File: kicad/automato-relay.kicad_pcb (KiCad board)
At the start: 2 copper layers, 308 x 75 mm, 51 parts, among them J1 TE-3-213598-4, J2 Screw_Terminal_01x03, J3 TE-3-213598-4, J4 Screw_Terminal_01x05, J5 TE-3-213598-4, J6 TE-3-213598-4, J7 Screw_Terminal_01x05, J8 TE-3-213598-4, K1 G5LE-14, K2 G5LE-14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

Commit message: layout: minor changes to appease DRC
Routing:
- net ACE: track 445.5 -> 448.6 mm
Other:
- net class EARTH: trace_width 0.25 -> 5; via_dia 0.8 -> 2; via_drill 0.4 -> 1
- net class HV: clearance 1.75 -> 1; trace_width 8 -> 5
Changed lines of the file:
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@@
     (thickness 1.6)
     (drawings 20)
-    (tracks 259)
+    (tracks 263)
     (zones 0)
     (modules 51)
@@
   (net_class EARTH ""
     (clearance 1)
-    (trace_width 0.25)
-    (via_dia 0.8)
-    (via_drill 0.4)
+    (trace_width 5)
+    (via_dia 2)
+    (via_drill 1)
     (uvia_dia 0.3)
     (uvia_drill 0.1)
@@
   )
   (net_class HV ""
-    (clearance 1.75)
-    (trace_width 8)
+    (clearance 1)
+    (trace_width 5)
     (via_dia 2)
     (via_drill 1)
@@
   (segment (start 34.08 152.92) (end 31.5 155.5) (width 2) (layer F.Cu) (net 9))
   (segment (start 44 152.92) (end 34.08 152.92) (width 2) (layer F.Cu) (net 9))
-  (segment (start 21.800001 163.800001) (end 25 167) (width 3) (layer F.Cu) (net 10))
-  (segment (start 25 102) (end 21.800001 105.199999) (width 3) (layer F.Cu) (net 10))
-  (segment (start 21.800001 105.199999) (end 21.800001 163.800001) (width 3) (layer F.Cu) (net 10))
   (segment (start 75 161) (end 75 153.38) (width 5) (layer F.Cu) (net 10))
   (segment (start 135 161) (end 135 153.38) (width 5) (layer F.Cu) (net 10))
@@
   (segment (start 44 158) (end 44 160) (width 3) (layer F.Cu) (net 10))
   (segment (start 325.47499 164.52501) (end 323 167) (width 3) (layer F.Cu) (net 10))
-  (segment (start 325.47499 104.47499) (end 325.47499 164.52501) (width 3) (layer F.Cu) (net 10))
-  (segment (start 323 102) (end 325.47499 104.47499) (width 3) (layer F.Cu) (net 10))
+  (segment (start 325.47499 104.47499) (end 325.47499 164.52501) (width 2) (layer F.Cu) (net 10))
+  (segment (start 25 102) (end 22.75 102) (width 2) (layer F.Cu) (net 10))
+  (segment (start 324.828432 102.99999) (end 325.97499 104.146548) (width 2) (layer F.Cu) (net 10))
+  (segment (start 323.99999 102.99999) (end 324.828432 102.99999) (width 2) (layer F.Cu) (net 10))
+  (segment (start 323 102) (end 323.99999 102.99999) (width 2) (layer F.Cu) (net 10))
+  (segment (start 22.02501 104.97499) (end 25 102) (width 2) (layer F.Cu) (net 10))
+  (segment (start 22.02501 165.189699) (end 22.02501 104.97499) (width 2) (layer F.Cu) (net 10))
+  (segment (start 23.835311 167) (end 22.02501 165.189699) (width 2) (layer F.Cu) (net 10))
+  (segment (start 25 167) (end 23.835311 167) (width 2) (layer F.Cu) (net 10))
   (segment (start 48 145) (end 48.749991 145.749991) (width 3) (layer B.Cu) (net 11))
   (segment (start 48 140) (end 48 145) (width 3) (layer B.Cu) (net 11))
@@
   (segment (start 64 117) (end 301 117) (width 1) (layer B.Cu) (net 17))
   (segment (start 64 127) (end 64 117) (width 1) (layer B.Cu) (net 17))
-  (segment (start 99.9625 120.0875) (end 100 120.05) (width 1) (layer F.Cu) (net 22))
-  (segment (start 97 120.0875) (end 99.9625 120.0875) (width 1) (layer F.Cu) (net 22))
   (segment (start 81.7875 120.0875) (end 93 120.0875) (width 0.6096) (layer F.Cu) (net 22))
   (segment (start 75.175 126.7) (end 81.7875 120.0875) (width 0.6096) (layer F.Cu) (net 22))
@@
   (segment (start 93.0875 120.0875) (end 91.9125 120.0875) (width 0.6096) (layer F.Cu) (net 22))
   (segment (start 97 120.0875) (end 93.0875 120.0875) (width 0.6096) (layer F.Cu) (net 22))
-  (segment (start 159.9625 120.0875) (end 160 120.05) (width 1) (layer F.Cu) (net 23))
-  (segment (start 157 120.0875) (end 159.9625 120.0875) (width 1) (layer F.Cu) (net 23))
+  (segment (start 97.0375 120.05) (end 97 120.0875) (width 0.6096) (layer F.Cu) (net 22))
+  (segment (start 100 120.05) (end 97.0375 120.05) (width 0.6096) (layer F.Cu) (net 22))
   (segment (start 76.445 122.425) (end 79.87 119) (width 0.6096) (layer F.Cu) (net 23))
   (segment (start 153.0875 120.0875) (end 157 120.0875) (width 0.6096) (layer F.Cu) (net 23))
@@
   (segment (start 149.175 124) (end 153.0875 120.0875) (width 0.6096) (layer F.Cu) (net 23))
   (segment (start 148 124) (end 149.175 124) (width 0.6096) (layer F.Cu) (net 23))
-  (segment (start 219.9625 120.0875) (end 220 120.05) (width 1) (layer F.Cu) (net 24))
-  (segment (start 217 120.0875) (end 219.9625 120.0875) (width 1) (layer F.Cu) (net 24))
+  (segment (start 159.9625 120.0875) (end 160 120.05) (width 0.6096) (layer F.Cu) (net 23))
+  (segment (start 157 120.0875) (end 159.9625 120.0875) (width 0.6096) (layer F.Cu) (net 23))
   (segment (start 211.13639 118.13639) (end 213.0875 120.0875) (width 0.6096) (layer F.Cu) (net 24))
   (segment (start 78.58861 118.13639) (end 211.13639 118.13639) (width 0.6096) (layer F.Cu) (net 24))
@@
   (segment (start 212.9125 120.0875) (end 213.0875 120.0875) (width 0.6096) (layer F.Cu) (net 24))
   (segment (start 209 124) (end 212.9125 120.0875) (width 0.6096) (layer F.Cu) (net 24))
-  (segment (start 279.9625 120.0875) (end 280 120.05) (width 1) (layer F.Cu) (net 25))
-  (segment (start 277 120.0875) (end 279.9625 120.0875) (width 1) (layer F.Cu) (net 25))
+  (segment (start 219.9625 120.0875) (end 220 120.05) (width 0.6096) (layer F.Cu) (net 24))
+  (segment (start 217 120.0875) (end 219.9625 120.0875) (width 0.6096) (layer F.Cu) (net 24))
   (segment (start 273.5125 120.0875) (end 277 120.0875) (width 0.6096) (layer F.Cu) (net 25))
   (segment (start 271.425 118) (end 273.5125 120.0875) (width 0.6096) (layer F.Cu) (net 25))
@@
   (segment (start 269.6 124) (end 273.5125 120.0875) (width 0.6096) (layer F.Cu) (net 25))
   (segment (start 268 124) (end 269.6 124) (width 0.6096) (layer F.Cu) (net 25))
+  (segment (start 277.0375 120.05) (end 277 120.0875) (width 0.6096) (layer F.Cu) (net 25))
+  (segment (start 280 120.05) (end 277.0375 120.05) (width 0.6096) (layer F.Cu) (net 25))
   (segment (start 100 144) (end 102 144) (width 1) (layer F.Cu) (net 30))
   (segment (start 102 144) (end 104 142) (width 1) (layer F.Cu) (net 30))
@@
     (polygon
       (pts
-        (xy 25.25 134.5) (xy 23.25 134.5) (xy 23.25 106) (xy 25.25 106)
+        (xy 324 134.75) (xy 322 134.75) (xy 322 105) (xy 324 105)
       )
     )
@@
     (polygon
       (pts
-        (xy 324 134.75) (xy 322 134.75) (xy 322 105) (xy 324 105)
+        (xy 25 134) (xy 23.25 134) (xy 23.25 106.5) (xy 25 106.5)
       )
     )

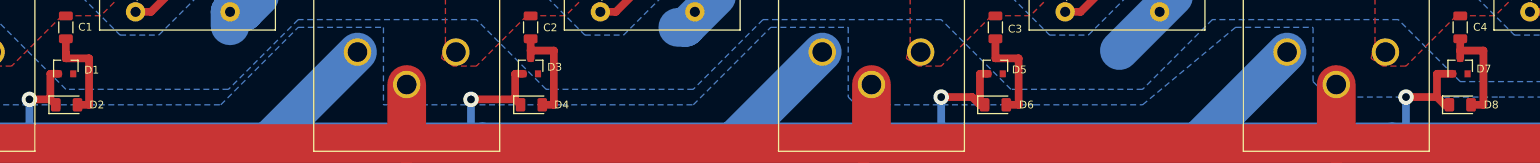
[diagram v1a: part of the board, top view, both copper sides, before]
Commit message: Changed indicator diode footprint and re-routed
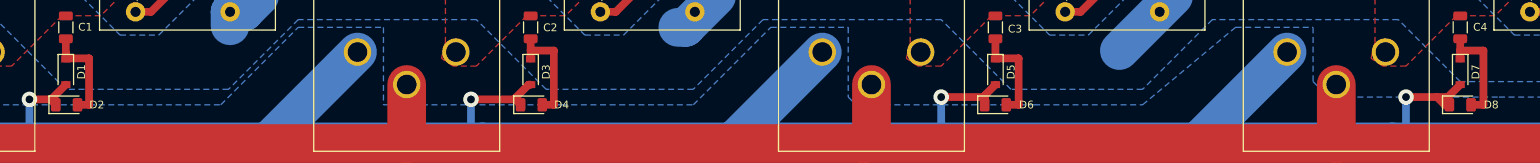
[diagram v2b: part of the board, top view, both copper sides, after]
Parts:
- D1, D3, D5, D7: footprint Diode_SMD:D_SOT-23_ANK -> Diode_SMD:D_SOD-123
- moved D1 0.75 mm to (91.0, 151.8), turned to 270 degrees
- moved D3 0.75 mm to (151.0, 151.8), turned to 270 degrees
- moved D5 0.75 mm to (211.0, 151.8), turned to 270 degrees
- moved D7 0.75 mm to (271.0, 151.8), turned to 270 degrees
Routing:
- net ACN: track 438.7 -> 432.7 mm

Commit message: Starting to play with pcb layout for new rev.
Moved outlets to top of board to make power switch placement more sensical.
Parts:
- added C9: 47n, Capacitor_SMD:C_1206_3216Metric, F.Cu at (161.5, 74.5)
- added D13: D, Diode_SMD:D_SOD-123, F.Cu at (161.6, 87.5)
- added D14: LED, LED_SMD:LED_1206_3216Metric, F.Cu at (130.4, 89.6)
- added SW1: SW_SPST, automato-relay:RA1H1C112R, F.Cu at (44.0, 110.5)
- J2: value Screw_Terminal_01x03 -> IEC-C14-FUSE; footprint Connector_Phoenix_MC_HighVoltage:PhoenixContact_MCV_1,5_3-G-5.08_1x03_P5.08mm_Vertical -> automato-relay:PF0011-15-PC
- moved D9 67.3 mm to (125.0, 188.5)
- moved Q1 67.3 mm to (126.0, 183.5)
- moved R5 67.3 mm to (122.0, 183.5)
- moved TP1 65.3 mm to (116.0, 183.0)
- moved J4 48.9 mm to (38.5, 63.0)
- moved C8 47.3 mm to (59.0, 107.0)
- moved C5 35.3 mm to (75.7, 91.2)
- moved C6 35.3 mm to (75.7, 94.0)
- moved J2 34.3 mm to (34.8, 125.0)
- moved J1 31.0 mm to (75.0, 119.0)
- moved J3 31.0 mm to (135.0, 119.0), turned to 180 degrees
- moved J5 31.0 mm to (195.0, 119.0), turned to 180 degrees
- moved J8 31.0 mm to (255.0, 119.0), turned to 180 degrees
- moved V1 30.0 mm to (51.0, 117.0), turned to 180 degrees
- moved U1 27.0 mm to (72.0, 152.0)
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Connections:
- J2 pad 1: ACE -> Net-(J2-Pad1)
- J2 pad 2: ACN -> ACE
- J2 pad 3: ACL -> ACN
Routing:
- net ACN: track 432.7 -> 72.7 mm, vias 4 -> 0
- net LATCH: track 345.1 -> 0.00 mm
- net CLK: track 341.3 -> 0.00 mm
- net ACE: track 448.6 -> 137.8 mm
- net SDO: track 286.7 -> 0.00 mm, vias 1 -> 0
- net CTRL4: track 217.3 -> 0.00 mm
- net CTRL3: track 154.6 -> 0.00 mm
- net CTRL2: track 92.1 -> 0.00 mm
- net GND: track 82.3 -> 15.3 mm
- net 3V3: track 97.1 -> 30.9 mm
- net SDI: track 57.6 -> 0.00 mm
- net ACL: track 84.0 -> 42.9 mm
- net CTRL1: track 36.3 -> 0.00 mm
- net Net-(C1-Pad2): track 13.0 -> 0.00 mm
- net Net-(D9-Pad2): track 29.7 -> 16.9 mm
- added copper zone on F.Cu, net Net-(J2-Pad1)
- removed copper zone on B.Cu, net ACL
- removed copper zone on B.Cu, net ACN
- removed copper zone on F.Cu, net Net-(C1-Pad1)

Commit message: routed high power section
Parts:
- moved C9 91.5 mm to (70.0, 75.0)
- moved D13 89.7 mm to (72.0, 82.5)
- moved C5 67.0 mm to (73.7, 158.2)
- moved C6 67.0 mm to (73.7, 161.0)
- moved D14 53.3 mm to (78.5, 77.5)
- moved D4 48.0 mm to (151.0, 108.0)
- moved D6 48.0 mm to (211.0, 108.0)
- moved D8 48.0 mm to (271.0, 108.0)
- moved D2 46.6 mm to (91.0, 108.0), turned to 0 degrees
- moved D1 43.9 mm to (91.0, 111.0), turned to 180 degrees
- moved D12 41.3 mm to (297.0, 88.4)
- moved Q4 41.3 mm to (298.0, 83.4)
- moved R7 41.3 mm to (294.0, 83.4)
- moved D3 40.8 mm to (151.0, 111.0), turned to 180 degrees
- moved D5 40.8 mm to (211.0, 111.0), turned to 180 degrees
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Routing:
- net ACE: track 137.8 -> 490.7 mm
- net ACN: track 72.7 -> 294.7 mm, vias 0 -> 4
- net ACL: track 42.9 -> 259.8 mm
- net Net-(C4-Pad1): track 0.00 -> 35.1 mm
- net Net-(C3-Pad1): track 0.00 -> 35.1 mm
- net Net-(C2-Pad1): track 0.00 -> 35.1 mm
- net Net-(C1-Pad1): track 0.00 -> 33.7 mm
- net Net-(D11-Pad2): track 29.7 -> 0.00 mm
- net Net-(D10-Pad2): track 29.7 -> 0.00 mm
- net Net-(D12-Pad2): track 29.7 -> 7.88 mm
- net 3V3: track 30.9 -> 17.9 mm
- net Net-(C4-Pad2): track 14.1 -> 5.71 mm
- net Net-(C2-Pad2): track 14.0 -> 5.87 mm
- net Net-(C3-Pad2): track 13.1 -> 5.87 mm
- net Net-(C1-Pad2): track 0.00 -> 5.50 mm
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- removed copper zone on F.Cu, net Net-(C2-Pad1)
- removed copper zone on F.Cu, net Net-(C3-Pad1)
- removed copper zone on F.Cu, net Net-(C4-Pad1)
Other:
- net class EARTH: clearance 1 -> 2; trace_width 5 -> 6
- net class HV: clearance 1 -> 2; trace_width 5 -> 6

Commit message: playing around with 5-pin connector location
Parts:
- J4: footprint automato-relay:PhoenixContact_1935190_1x5 -> Connector_JST:JST_EH_S5B-EH_1x05_P2.50mm_Horizontal
- moved J4 103.1 mm to (87.0, 154.0), turned to 180 degrees
- moved C7 73.5 mm to (71.0, 153.0)
- moved D9 57.7 mm to (101.0, 136.0), turned to 180 degrees
- moved R7 57.0 mm to (287.4, 140.0), turned to 0 degrees
- moved Q4 53.7 mm to (287.4, 136.0), turned to 90 degrees
- moved Q1 51.0 mm to (106.2, 136.5), turned to 90 degrees
- moved D12 49.9 mm to (282.0, 136.0), turned to 180 degrees
- moved TP1 46.1 mm to (97.0, 141.0)
- moved R5 45.8 mm to (106.2, 140.5), turned to 0 degrees
- moved J7 41.1 mm to (334.0, 161.0)
- moved R4 40.7 mm to (227.4, 140.2), turned to 0 degrees
- moved TP2 37.9 mm to (158.0, 141.0)
- moved Q3 37.3 mm to (227.4, 136.2), turned to 90 degrees
- moved D11 24.2 mm to (222.0, 136.0), turned to 180 degrees
- moved TP3 19.7 mm to (218.0, 141.0)
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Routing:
- net CTRL4: track 0.00 -> 216.9 mm
- net CTRL3: track 0.00 -> 155.1 mm
- net ACE: track 490.7 -> 360.5 mm
- net CTRL2: track 0.00 -> 96.0 mm
- net 3V3: track 17.9 -> 64.0 mm, vias 1 -> 0
- net CTRL1: track 0.00 -> 36.0 mm
- net Net-(D11-Pad2): track 0.00 -> 17.8 mm
- net Net-(D10-Pad2): track 0.00 -> 17.5 mm
- net Net-(D12-Pad2): track 7.88 -> 17.7 mm
- net GND: track 12.4 -> 21.3 mm
- net Net-(D9-Pad2): track 16.9 -> 18.3 mm
- net SDI: track 0.00 -> 0.88 mm
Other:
- outline, holes or cut-outs redrawn
- net class Default: clearance 0.254 -> 0.2032; trace_width 0.25 -> 0.2032
- rule trace_clearance: 0.254 -> 0.2032

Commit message: add usb-c receptacles, begin digital routing
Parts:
- J4: value Screw_Terminal_01x05 -> USB_C_Receptacle_USB2.0; footprint Connector_JST:JST_EH_S5B-EH_1x05_P2.50mm_Horizontal -> automato-relay:USB_C_Receptacle_GCT-USB4105
- J7: value Screw_Terminal_01x05 -> USB_C_Receptacle_USB2.0; footprint automato-relay:PhoenixContact_1935190_1x5 -> automato-relay:USB_C_Receptacle_GCT-USB4105
- moved J4 52.0 mm to (35.0, 153.1), turned to 0 degrees
- moved C9 37.7 mm to (55.0, 109.6), turned to 90 degrees
- moved D13 27.4 mm to (57.0, 105.4)
- moved J7 21.2 mm to (324.0, 142.2)
- moved D14 13.3 mm to (67.6, 85.2), turned to 180 degrees
- moved PS1 2.60 mm to (54.6, 123.2)
- moved V1 1.20 mm to (52.2, 117.6)
- moved C8 0.63 mm to (59.6, 107.8)
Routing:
- net GND: track 21.3 -> 350.4 mm, vias 0 -> 5
- net 3V3: track 64.0 -> 381.5 mm
- net CLK: track 0.00 -> 58.1 mm
- net LATCH: track 0.00 -> 55.5 mm
- net SDI: track 0.88 -> 52.9 mm, vias 0 -> 2
- net CTRL3: track 155.1 -> 166.9 mm
- net CTRL2: track 96.0 -> 107.5 mm
- net CTRL4: track 216.9 -> 225.8 mm
- net CTRL1: track 36.0 -> 44.5 mm
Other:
- board text removed: "3V3"
- board text removed: "SDI"

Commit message: finished routing logic
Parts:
- moved D14 19.6 mm to (57.2, 101.8)
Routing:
- net ACE: track 360.5 -> 65.2 mm
- net LATCH: track 55.5 -> 313.5 mm, vias 0 -> 2
- net CLK: track 58.1 -> 312.8 mm, vias 0 -> 2
- net SDO: track 0.00 -> 246.2 mm, vias 0 -> 2
- net ACN: track 294.7 -> 363.5 mm
- net GND: track 350.4 -> 378.0 mm, vias 5 -> 7
- net ACL: track 259.8 -> 283.4 mm
- net 3V3: track 381.5 -> 392.5 mm, vias 0 -> 1

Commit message: mostly finished power routing
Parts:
- moved D13 243.1 mm to (300.0, 113.4), turned to 270 degrees
- moved D14 240.7 mm to (297.8, 108.6)
- moved C9 240.6 mm to (295.6, 113.4)
- moved REF** 4.46 mm to (322.8, 151.8)
- moved J7 0.60 mm to (324.0, 141.7)
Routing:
- net ACN: track 363.5 -> 394.9 mm, vias 4 -> 5
- net ACL: track 283.4 -> 308.2 mm
- net Net-(C9-Pad2): track 0.00 -> 10.5 mm
- net 3V3: track 392.5 -> 399.1 mm
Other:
- board size 308 x 75 mm -> 308 x 60 mm
